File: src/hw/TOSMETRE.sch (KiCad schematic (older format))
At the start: 44 parts, among them J2 Conn_Coaxial, J3 Conn_01x08_Male, J4 Barrel_Jack_Switch, J5 Conn_Coaxial, J6 Alim Piles, SW1 SW_Push, SW2 SW_Push_Dual_x2, SW3 SW_DIP_x01, U1 18F1320, U3 LT1818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

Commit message: #343 modif aop
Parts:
- added D?: BAT54XV2, Diode_SMD:D_SOD-523, symbol librairie_projet:BAT54XV2
- added R? (x2): 625, Resistor_SMD:R_1206_3216Metric, symbol Device:R
- R1, R4: value 625 -> 100
- R5, R6: value 625 -> 1000
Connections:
- wire segments 187 -> 201
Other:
- note removed: "pont\n\n"
- note removed: "résistance\ntest AOP1\n"
- moved on the sheet: C8, D1, D2, D3, J2, J5, R1, R10, R4, R5, R9

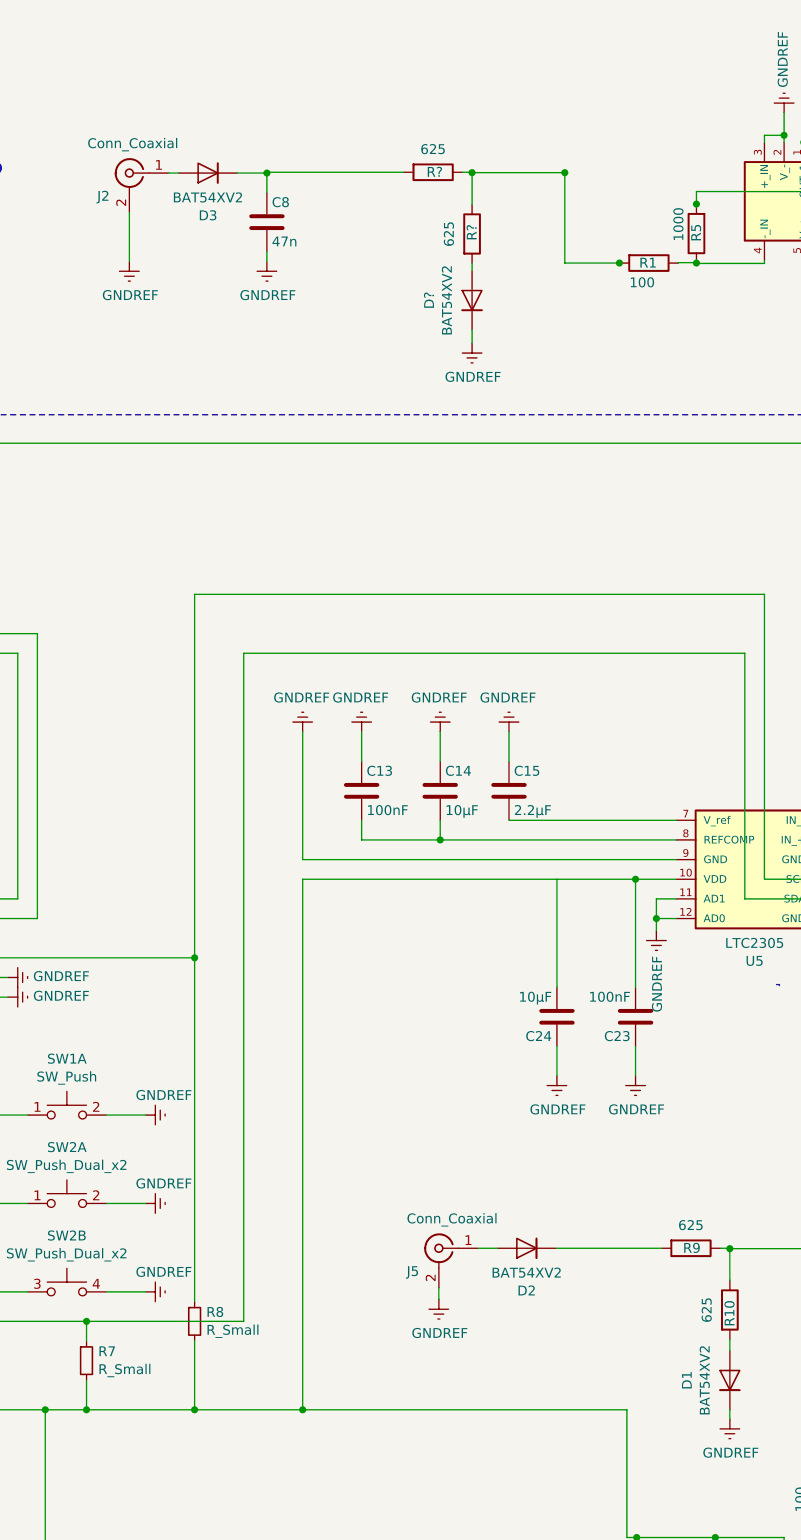
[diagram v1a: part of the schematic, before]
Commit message: #333 adaptation 50 ohms
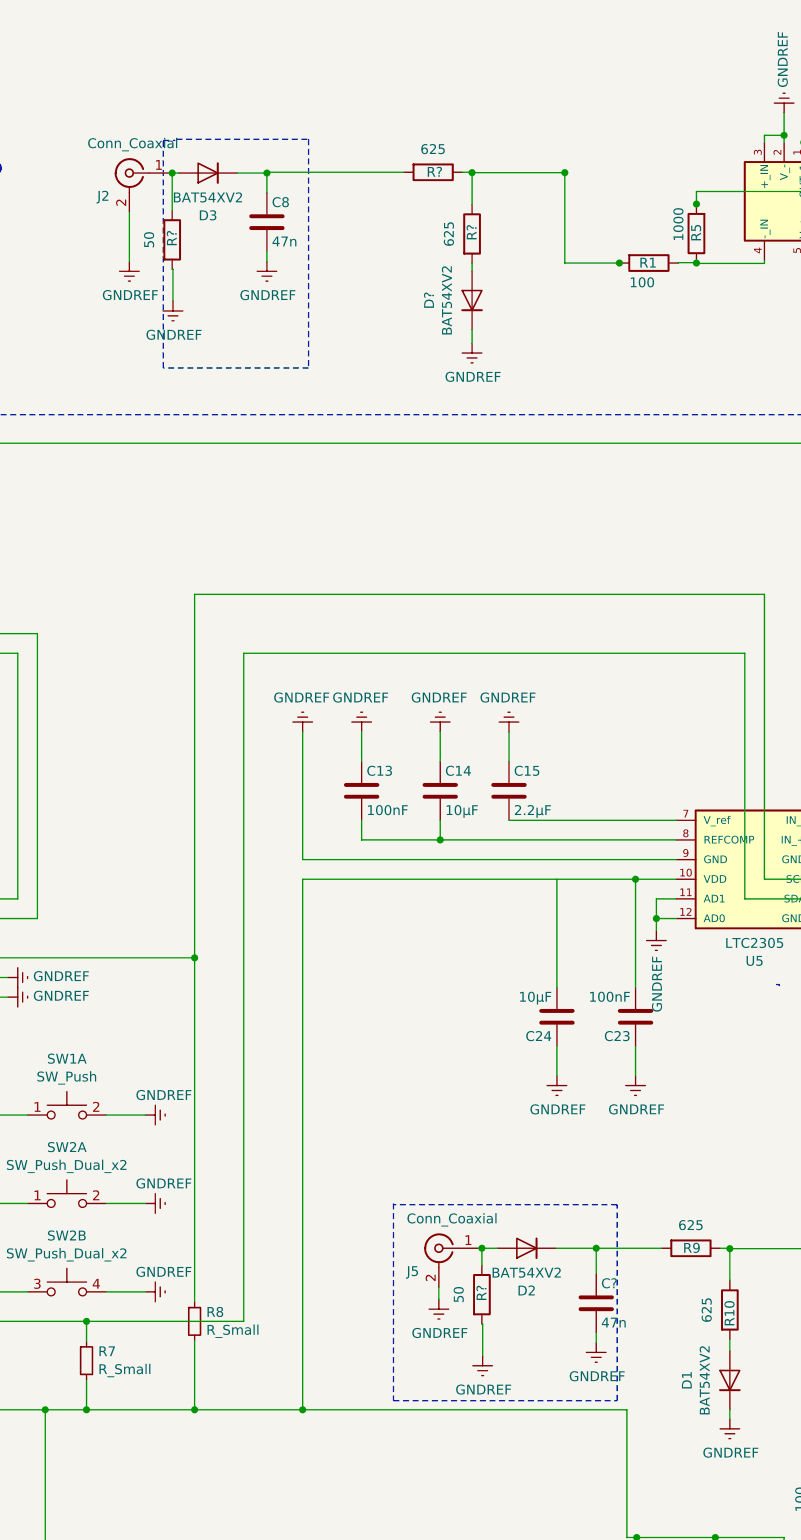
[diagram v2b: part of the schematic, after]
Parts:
- added C?: 47n, Capacitor_SMD:C_1206_3216Metric, symbol Device:C
- added R? (x2): 50, Resistor_SMD:R_1206_3216Metric, symbol Device:R
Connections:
- wire segments 201 -> 212
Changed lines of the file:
@@
 	6718 2206 6868 2206
 Wire Wire Line
-	6368 2206 6418 2206
+	6368 2206 6386 2206
 Wire Wire Line
 	9500 2050 9500 2014
@@
 $EndComp
 Wire Wire Line
-	7943 7678 8040 7678
-Wire Wire Line
-	8340 7678 8876 7678
+	7943 7678 7962 7678
+Wire Wire Line
+	8340 7678 8544 7678
 $Comp
 L Device:R R9
@@
 	6868 2202 7564 2202
 Connection ~ 6868 2206
+$Comp
+L Device:R R?
+U 1 1 60409738
+P 6386 2546
+F 0 "R?" V 6386 2596 50  0000 R CNN
+F 1 "50" V 6270 2546 50  0000 C CNN
+F 2 "Resistor_SMD:R_1206_3216Metric" V 6316 2546 50  0001 C CNN
+F 3 "~" H 6386 2546 50  0001 C CNN
+	1    6386 2546
+	1    0    0    -1
+$EndComp
+$Comp
+L power:GNDREF #PWR?
+U 1 1 60415265
+P 6390 2858
+F 0 "#PWR?" H 6390 2608 50  0001 C CNN
+F 1 "GNDREF" H 6395 2685 50  0000 C CNN
+F 2 "" H 6390 2858 50  0001 C CNN
+F 3 "" H 6390 2858 50  0001 C CNN
+	1    6390 2858
+	1    0    0    -1
+$EndComp
+Wire Wire Line
+	6390 2858 6390 2696
+Wire Wire Line
+	6390 2696 6386 2696
+Wire Wire Line
+	6386 2396 6386 2206
+Connection ~ 6386 2206
+Wire Wire Line
+	6386 2206 6418 2206
+$Comp
+L Device:R R?
+U 1 1 60441AE1
+P 7962 7914
+F 0 "R?" V 7962 7964 50  0000 R CNN
+F 1 "50" V 7846 7914 50  0000 C CNN
+F 2 "Resistor_SMD:R_1206_3216Metric" V 7892 7914 50  0001 C CNN
+F 3 "~" H 7962 7914 50  0001 C CNN
+	1    7962 7914
+	1    0    0    -1
+$EndComp
+$Comp
+L power:GNDREF #PWR?
+U 1 1 60441AEB
+P 7966 8226
+F 0 "#PWR?" H 7966 7976 50  0001 C CNN
+F 1 "GNDREF" H 7971 8053 50  0000 C CNN
+F 2 "" H 7966 8226 50  0001 C CNN
+F 3 "" H 7966 8226 50  0001 C CNN
+	1    7966 8226
+	1    0    0    -1
+$EndComp
+Wire Wire Line
+	7966 8226 7966 8064
+Wire Wire Line
+	7966 8064 7962 8064
+Wire Wire Line
+	7962 7764 7962 7678
+Connection ~ 7962 7678
+Wire Wire Line
+	7962 7678 8040 7678
+$Comp
+L Device:C C?
+U 1 1 6045ADE2
+P 8544 7958
+F 0 "C?" H 8569 8058 50  0000 L CNN
+F 1 "47n" H 8569 7858 50  0000 L CNN
+F 2 "Capacitor_SMD:C_1206_3216Metric" H 8582 7808 50  0001 C CNN
+F 3 "" H 8544 7958 50  0001 C CNN
+	1    8544 7958
+	1    0    0    -1
+$EndComp
+Wire Wire Line
+	8544 8108 8544 8158
+$Comp
+L power:GNDREF #PWR?
+U 1 1 6045ADED
+P 8544 8158
+F 0 "#PWR?" H 8544 7908 50  0001 C CNN
+F 1 "GNDREF" H 8549 7985 50  0000 C CNN
+F 2 "" H 8544 8158 50  0001 C CNN
+F 3 "" H 8544 8158 50  0001 C CNN
+	1    8544 8158
+	1    0    0    -1
+$EndComp
+Wire Wire Line
+	8544 7808 8544 7678
+Connection ~ 8544 7678
+Wire Wire Line
+	8544 7678 8876 7678
+Wire Notes Line
+	7512 7450 7512 8454
+Wire Notes Line
+	7512 8454 8650 8454
+Wire Notes Line
+	8650 8454 8650 7456
+Wire Notes Line
+	8650 7456 7512 7456
+Wire Notes Line
+	6408 2034 7080 2034
+Wire Notes Line
+	7080 2034 7080 3198
+Wire Notes Line
+	7080 3198 6340 3198
+Wire Notes Line
+	6340 3198 6340 2040
+Wire Notes Line
+	6340 2040 6402 2040
 $EndSCHEMATC

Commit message: #274 bouton calibration + -
modif libelle boutons calibration
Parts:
- SW2: value SW_Push_Dual_x2 -> calibration -
- SW2: value SW_Push_Dual_x2 -> calibration +
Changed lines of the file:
@@
 P 5850 7450
 F 0 "SW2" H 5850 7735 50  0000 C CNN
-F 1 "SW_Push_Dual_x2" H 5850 7644 50  0000 C CNN
+F 1 "calibration -" H 5850 7644 50  0000 C CNN
 F 2 "Button_Switch_SMD:SW_Push_1P1T-SH_NO_CK_KMR2xxG" H 5850 7650 50  0001 C CNN
 F 3 "~" H 5850 7650 50  0001 C CNN
@@
 P 5850 7900
 F 0 "SW2" H 5850 8185 50  0000 C CNN
-F 1 "SW_Push_Dual_x2" H 5850 8094 50  0000 C CNN
+F 1 "calibration +" H 5850 8094 50  0000 C CNN
 F 2 "Button_Switch_SMD:SW_Push_1P1T-SH_NO_CK_KMR2xxG" H 5850 8100 50  0001 C CNN
 F 3 "~" H 5850 8100 50  0001 C CNN
@@
 Wire Notes Line
 	6340 2040 6402 2040
+Wire Notes Line
+	5334 7106 6124 7106
+Wire Notes Line
+	6124 7106 6124 7968
+Wire Notes Line
+	6124 7968 5330 7968
+Wire Notes Line
+	5330 7968 5330 7110
 $EndSCHEMATC

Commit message: # modif libelle bouton freq
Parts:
- SW1: value SW_Push -> change frequence
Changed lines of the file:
@@
 P 5850 7000
 F 0 "SW1" H 5850 7285 50  0000 C CNN
-F 1 "SW_Push" H 5850 7194 50  0000 C CNN
+F 1 "change frequence" H 5850 7194 50  0000 C CNN
 F 2 "Button_Switch_SMD:SW_Push_1P1T-SH_NO_CK_KMR2xxG" H 5850 7200 50  0001 C CNN
 F 3 "~" H 5850 7200 50  0001 C CNN

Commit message: #350
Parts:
- removed C5: CP_Small, Capacitor_SMD:C_1206_3216Metric, symbol Device:CP_Small
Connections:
- wire segments 212 -> 210
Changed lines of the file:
@@
 EESchema Schematic File Version 4
-LIBS:TOSMETRE-cache
-EELAYER 29 0
+EELAYER 30 0
 EELAYER END
 $Descr A3 16535 11693
@@
 $EndComp
 Wire Wire Line
-	2250 6700 2250 6800
-Wire Wire Line
 	4400 6300 3950 6300
 Connection ~ 3950 6400
 Wire Wire Line
 	3950 6300 3950 6400
-$Comp
-L power:GNDREF #PWR01
-U 1 1 5A343ADA
-P 2250 6800
-F 0 "#PWR01" H 2250 6550 50  0001 C CNN
-F 1 "GNDREF" V 2250 6650 50  0000 R CNN
-F 2 "" H 2250 6800 50  0001 C CNN
-F 3 "" H 2250 6800 50  0001 C CNN
-	1    2250 6800
-	1    0    0    -1
-$EndComp
-$Comp
-L Device:CP_Small C5
-U 1 1 5AA53058
-P 2250 6600
-F 0 "C5" H 2260 6670 50  0000 L CNN
-F 1 "CP_Small" H 2260 6520 50  0000 L CNN
-F 2 "Capacitor_SMD:C_1206_3216Metric" H 2250 6600 50  0001 C CNN
-F 3 "" H 2250 6600 50  0001 C CNN
-	1    2250 6600
-	1    0    0    -1
-$EndComp
-Wire Wire Line
-	2250 6500 2250 6400
 $Comp
 L Device:R R3
@@
 Wire Wire Line
 	2250 3580 2250 3581
-Connection ~ 2250 6400
 Connection ~ 2250 3581
 Wire Wire Line

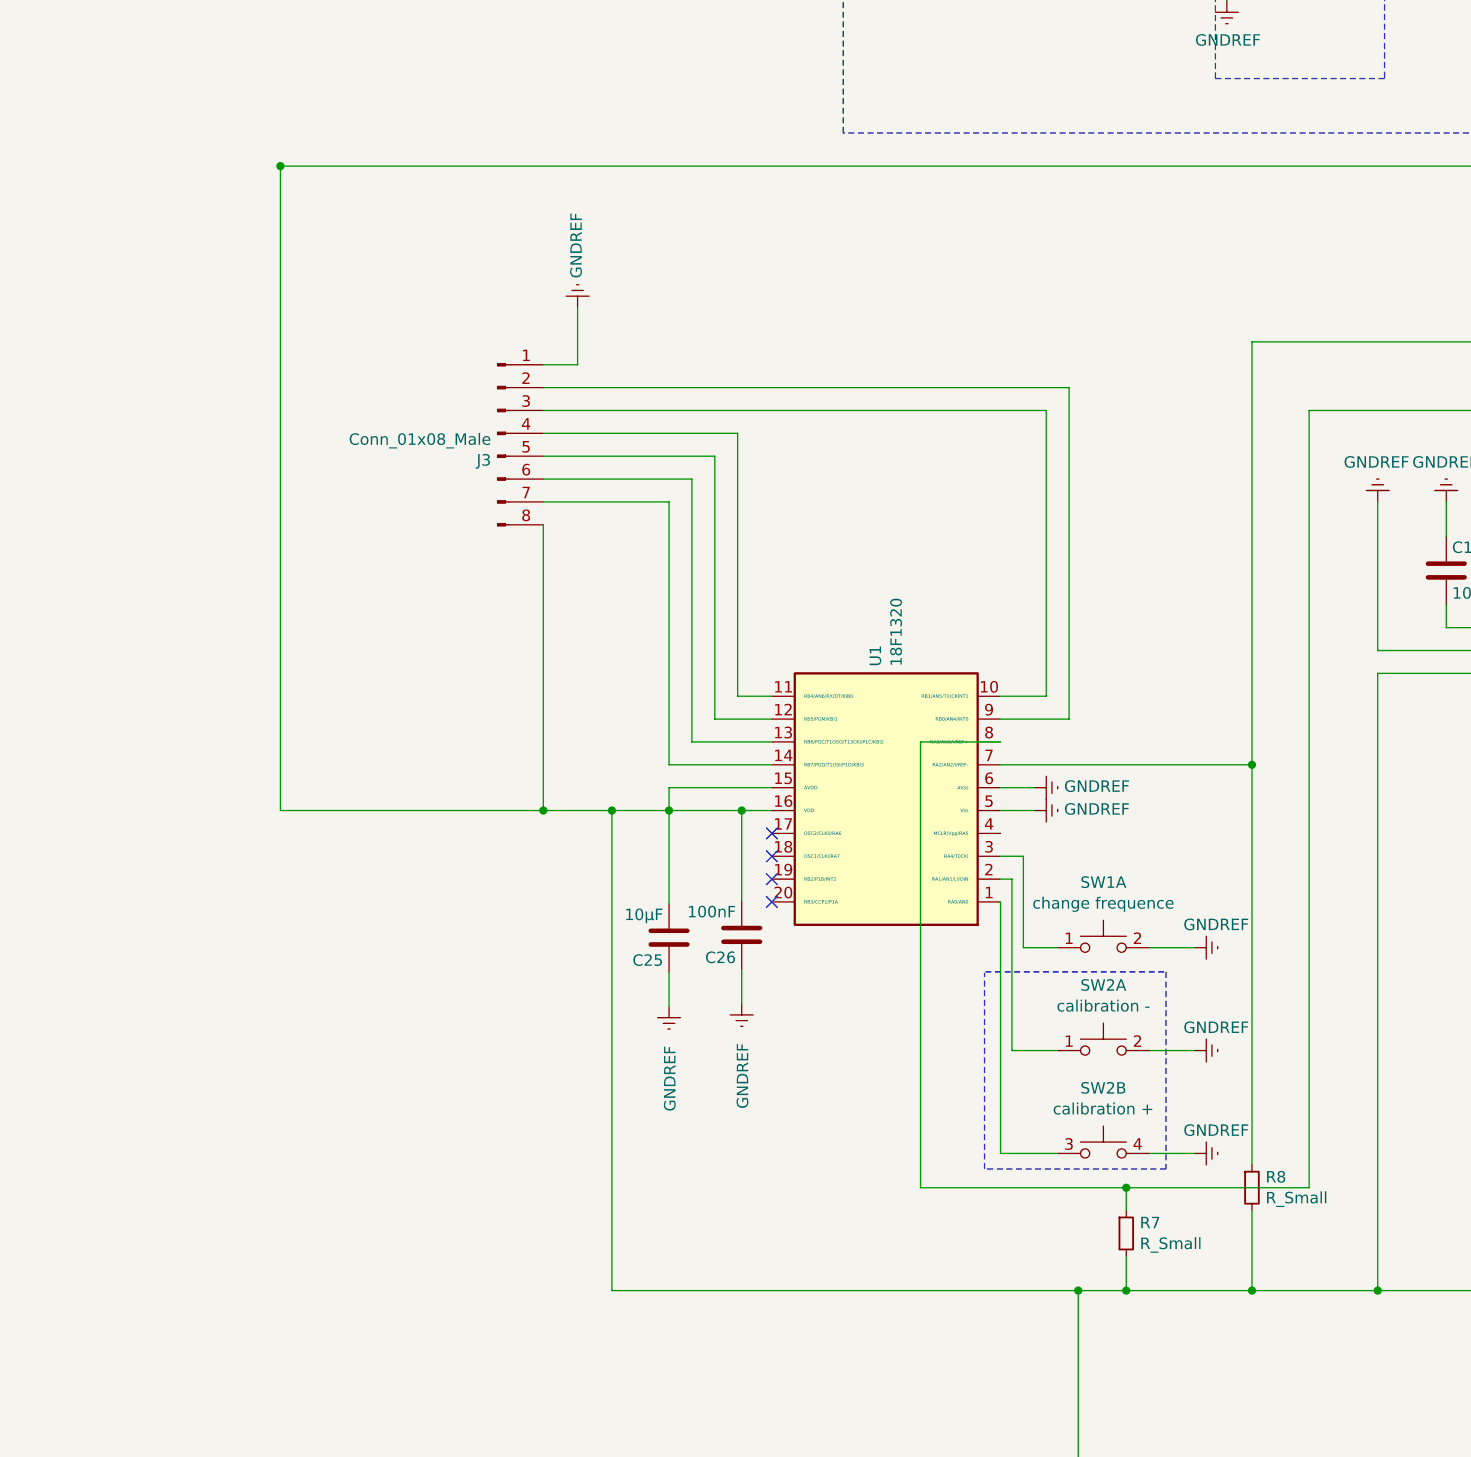
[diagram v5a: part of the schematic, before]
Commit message: #274 boutons calibrations supprimes
pullup  sur bouton bande
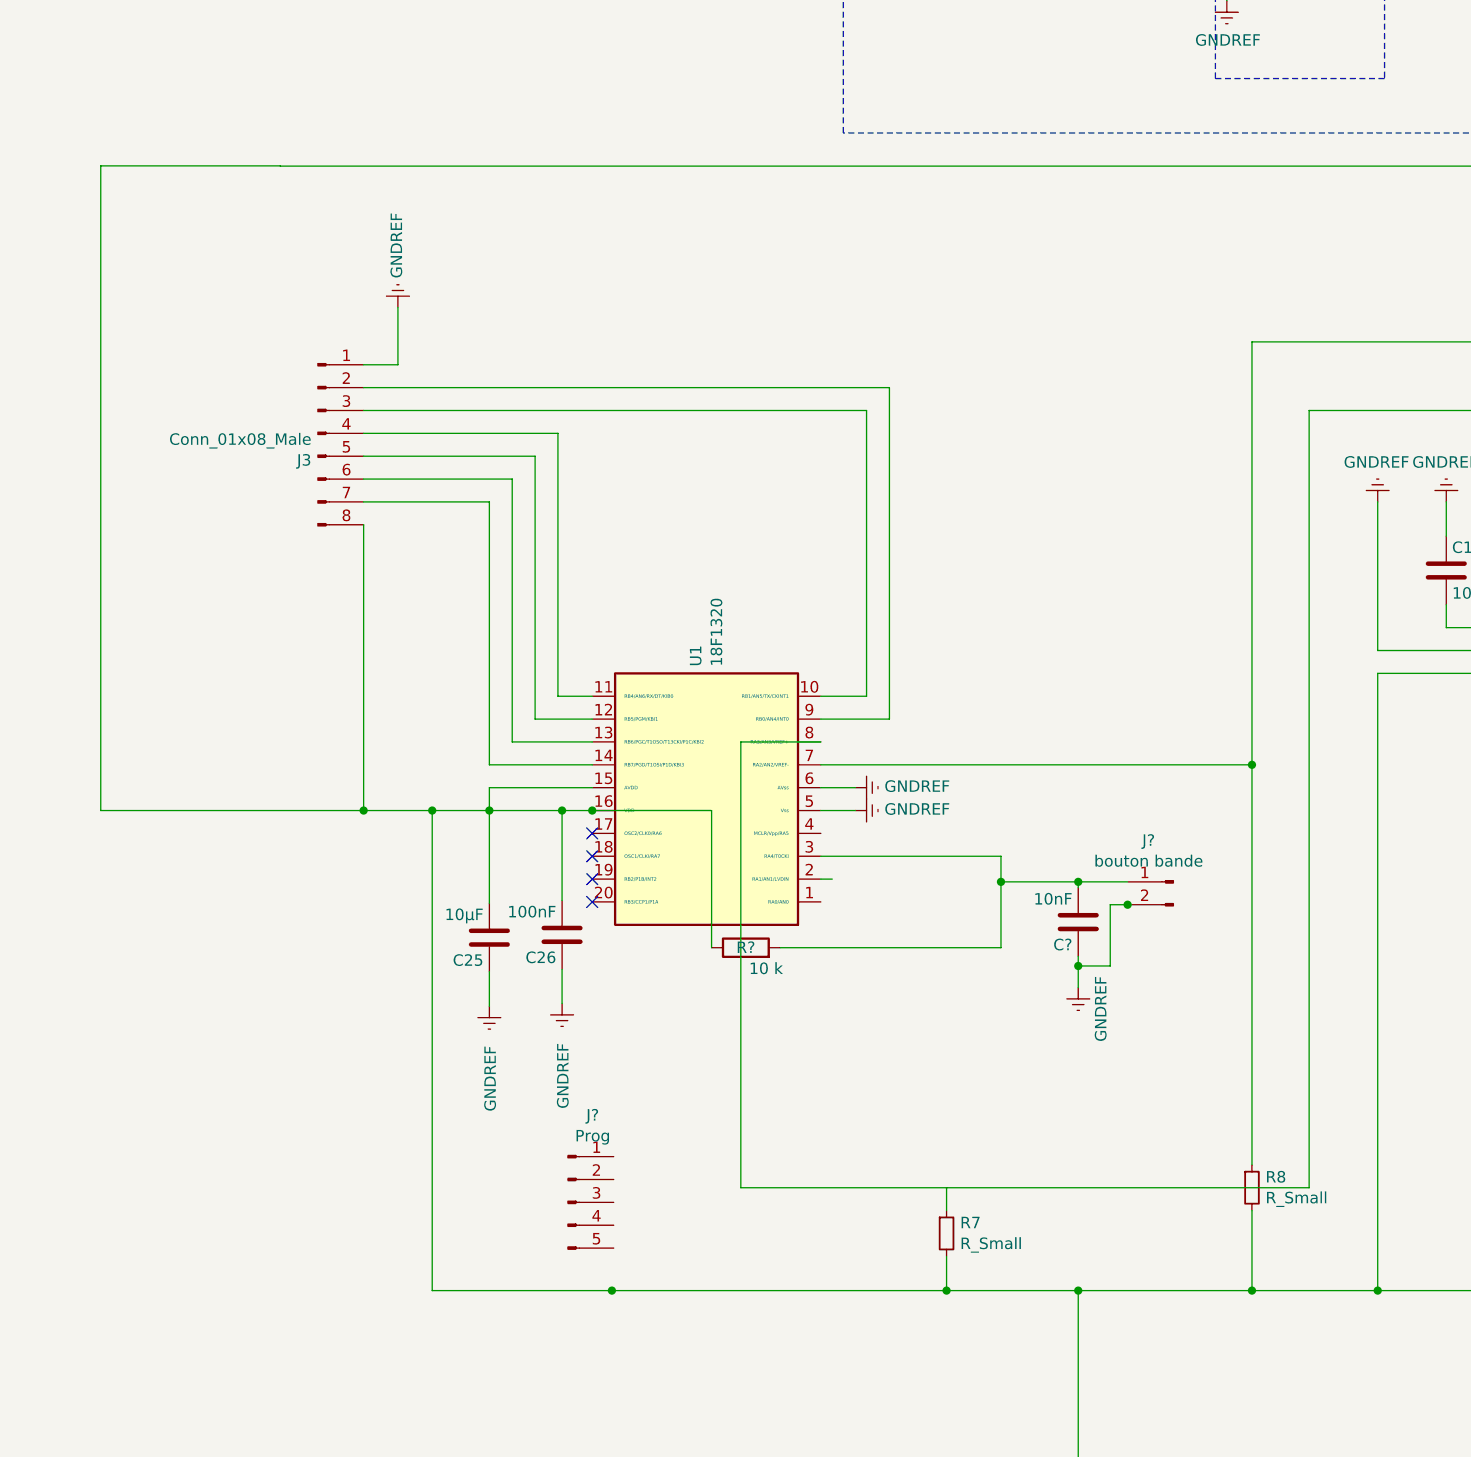
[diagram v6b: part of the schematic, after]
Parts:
- removed SW1: change frequence, Button_Switch_SMD:SW_Push_1P1T-SH_NO_CK_KMR2xxG, symbol Switch:SW_Push_Dual_x2
- removed SW2: calibration -, Button_Switch_SMD:SW_Push_1P1T-SH_NO_CK_KMR2xxG, symbol Switch:SW_Push_Dual_x2
- added C?: 10nF, Capacitor_SMD:C_1206_3216Metric, symbol Device:C
- added J?: bouton bande, symbol Connector:Conn_01x02_Male
- added J?: Prog, symbol Connector:Conn_01x05_Male
- added R?: 10 k, Resistor_SMD:R_1206_3216Metric, symbol Device:R
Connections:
- wire segments 210 -> 217
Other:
- moved on the sheet: C25, C26, J3, R7, U1
